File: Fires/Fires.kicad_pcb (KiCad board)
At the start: 2 copper layers, 76.2 x 12.7 mm, 13 parts, among them J1 Power

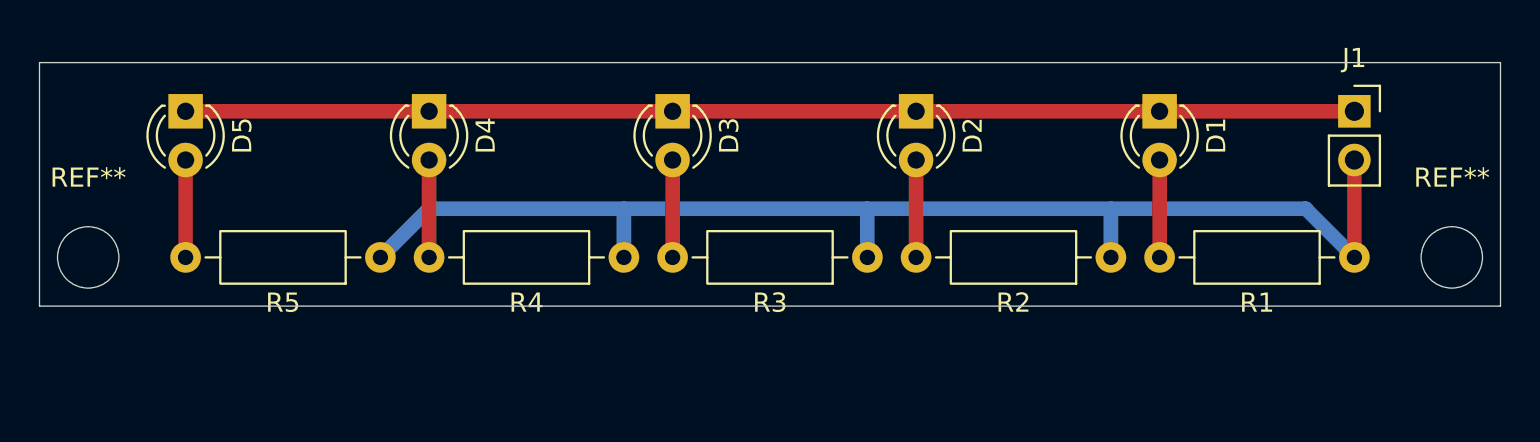
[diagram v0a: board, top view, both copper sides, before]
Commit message: 出力を追加
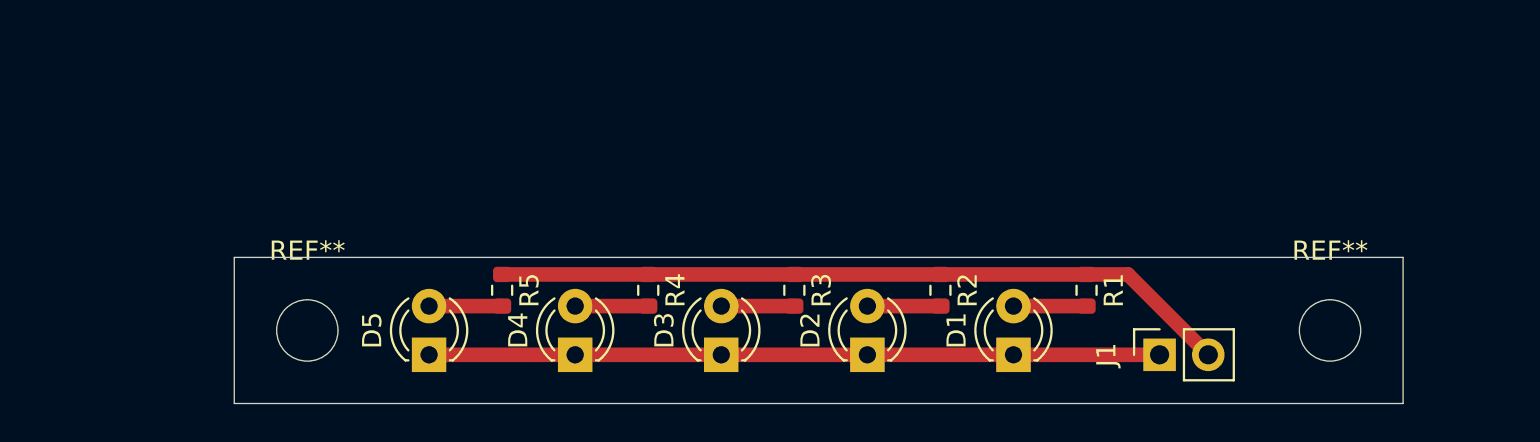
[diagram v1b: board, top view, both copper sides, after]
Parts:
- removed the REF** at (116.8, 76.2)
- removed the REF** at (188.0, 76.2)
- added REF**: MountingHole_3.2mm_M3, MountingHole:MountingHole_3.2mm_M3, F.Cu at (128.3, 80.0)
- added REF**: MountingHole_3.2mm_M3, MountingHole:MountingHole_3.2mm_M3, F.Cu at (181.6, 80.0)
- J1: value Power -> PowerSocket
- R1, R2, R3, R4, R5: value 68 -> 100; footprint Resistor_THT:R_Axial_DIN0207_L6.3mm_D2.5mm_P10.16mm_Horizontal -> Resistor_SMD:R_0603_1608Metric
- moved D5 18.0 mm to (134.6, 81.3), turned to 90 degrees
- moved J1 16.3 mm to (172.7, 81.3), turned to 90 degrees
- moved D1 14.8 mm to (165.1, 81.3), turned to 90 degrees
- moved D4 14.8 mm to (142.2, 81.3), turned to 90 degrees
- moved R1 14.1 mm to (168.9, 77.9), turned to -90 degrees
- moved D2 13.0 mm to (157.5, 81.3), turned to 90 degrees
- moved D3 13.0 mm to (149.9, 81.3), turned to 90 degrees
- moved R2 9.05 mm to (161.3, 77.9), turned to -90 degrees
- moved R5 6.58 mm to (138.4, 77.9), turned to -90 degrees
- moved R3 4.18 mm to (153.7, 77.9), turned to -90 degrees
- moved R4 2.13 mm to (146.1, 77.9), turned to -90 degrees
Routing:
- net GND: track 121.9 -> 38.1 mm
- net VCC: track 111.3 -> 38.6 mm
- net Net-(D3-A): track 5.08 -> 3.81 mm
- net Net-(D5-A): track 5.08 -> 3.81 mm
- net Net-(D4-A): track 5.08 -> 3.81 mm
- net Net-(D2-A): track 5.08 -> 3.81 mm
- net Net-(D1-A): track 5.08 -> 3.81 mm
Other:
- board size 76.2 x 12.7 mm -> 61 x 7.6 mm
